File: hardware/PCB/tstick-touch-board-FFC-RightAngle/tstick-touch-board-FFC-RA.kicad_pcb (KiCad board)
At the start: 2 copper layers, 85.6 x 31.8 mm, 14 parts, among them J1 Conn_01x32

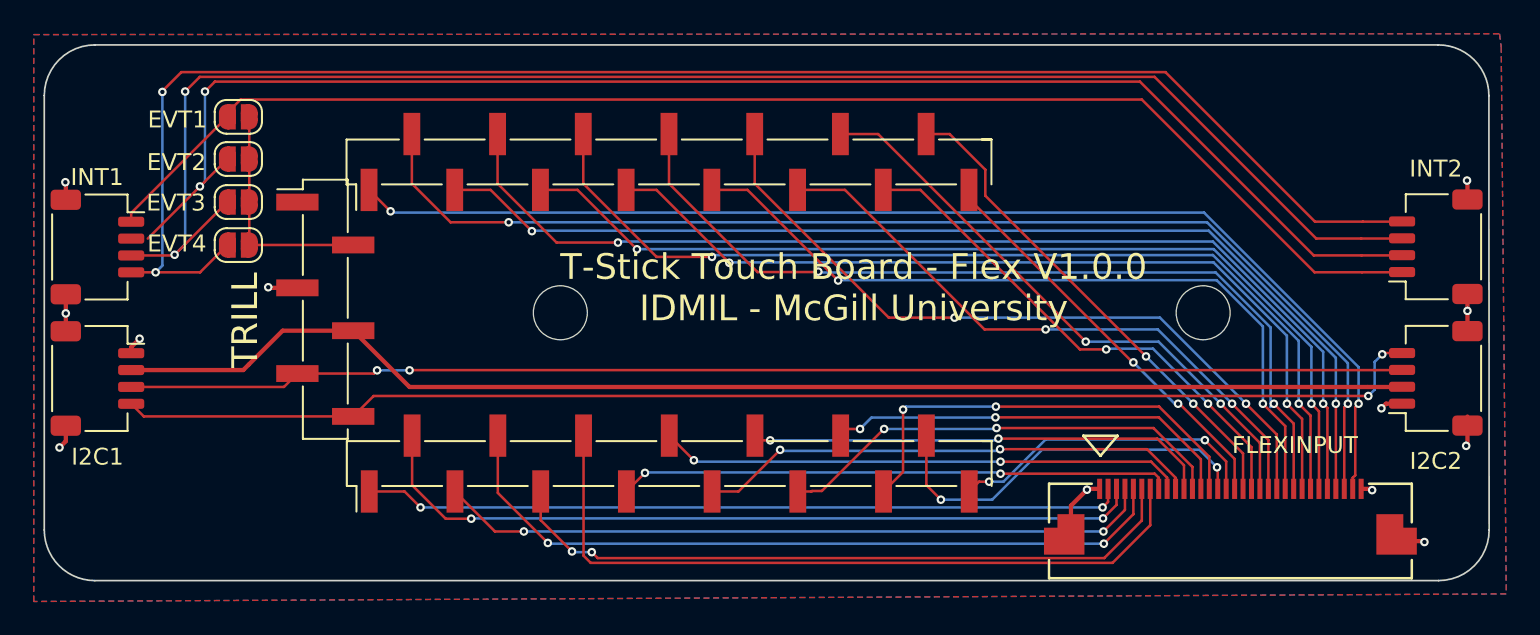
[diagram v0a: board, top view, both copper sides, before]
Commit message: cleaned up v1 of the boards, fixed issue with evt2 trace not being connected in touch board
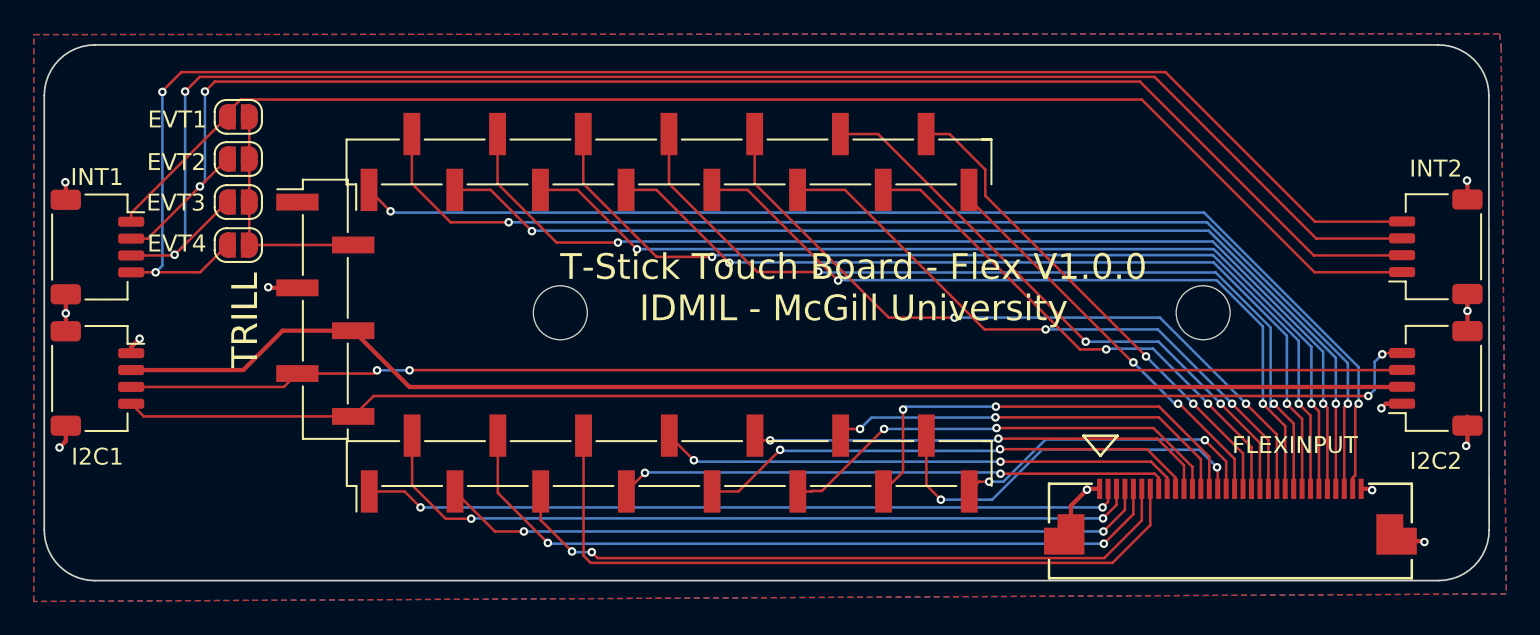
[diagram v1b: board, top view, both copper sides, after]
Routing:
- net /EVT2: track 87.9 -> 88.9 mm
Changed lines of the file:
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@@
     (descr "JST SH series connector, SM04B-SRSS-TB (http://www.jst-mfg.com/product/pdf/eng/eSH.pdf), generated with kicad-footprint-generator")
     (tags "connector JST SH top entry")
+    (property "Alternate Part #" "")
+    (property "Description Value Pkg" "Connector Header Surface Mount, Right Angle 4 position 0.039\" (1.00mm)")
+    (property "Digikey Part #" "455-SM04B-SRSS-TBCT-ND")
+    (property "Mfg Part #" "SM04B-SRSS-TB")
     (property "Sheetfile" "tstick-touch-board-FFC-RA.kicad_sch")
     (property "Sheetname" "")
@@
     (descr "JST SH series connector, SM04B-SRSS-TB (http://www.jst-mfg.com/product/pdf/eng/eSH.pdf), generated with kicad-footprint-generator")
     (tags "connector JST SH top entry")
+    (property "Alternate Part #" "")
+    (property "Description Value Pkg" "Connector Header Surface Mount, Right Angle 4 position 0.039\" (1.00mm)")
+    (property "Digikey Part #" "455-SM04B-SRSS-TBCT-ND")
+    (property "Mfg Part #" "SM04B-SRSS-TB")
     (property "Sheetfile" "tstick-touch-board-FFC-RA.kicad_sch")
     (property "Sheetname" "")
@@
     (descr "JST SH series connector, SM04B-SRSS-TB (http://www.jst-mfg.com/product/pdf/eng/eSH.pdf), generated with kicad-footprint-generator")
     (tags "connector JST SH top entry")
+    (property "Alternate Part #" "")
+    (property "Description Value Pkg" "Connector Header Surface Mount, Right Angle 4 position 0.039\" (1.00mm)")
+    (property "Digikey Part #" "455-SM04B-SRSS-TBCT-ND")
+    (property "Mfg Part #" "SM04B-SRSS-TB")
     (property "Sheetfile" "tstick-touch-board-FFC-RA.kicad_sch")
     (property "Sheetname" "")
@@
     (descr "JST SH series connector, SM04B-SRSS-TB (http://www.jst-mfg.com/product/pdf/eng/eSH.pdf), generated with kicad-footprint-generator")
     (tags "connector JST SH top entry")
+    (property "Alternate Part #" "")
+    (property "Description Value Pkg" "Connector Header Surface Mount, Right Angle 4 position 0.039\" (1.00mm)")
+    (property "Digikey Part #" "455-SM04B-SRSS-TBCT-ND")
+    (property "Mfg Part #" "SM04B-SRSS-TB")
     (property "Sheetfile" "tstick-touch-board-FFC-RA.kicad_sch")
     (property "Sheetname" "")
@@
   (segment (start 144.7697 90.1075) (end 144.7642 90.113) (width 0.1524) (layer "F.Cu") (net 32))
   (segment (start 137.7642 88.213) (end 137.7642 88.729) (width 0.1524) (layer "F.Cu") (net 33))
-  (segment (start 143.3392 82.513) (end 143.4642 82.513) (width 0.1524) (layer "F.Cu") (net 33))
   (segment (start 213.0772 91.725) (end 213.0892 91.713) (width 0.1524) (layer "F.Cu") (net 33))
   (segment (start 144.249002 81.488) (end 143.4642 82.272802) (width 0.1524) (layer "F.Cu") (net 33))
@@
   (segment (start 143.4642 82.513) (end 137.7642 88.213) (width 0.1524) (layer "F.Cu") (net 33))
   (segment (start 197.6642 81.488) (end 144.249002 81.488) (width 0.1524) (layer "F.Cu") (net 33))
-  (segment (start 210.7142 91.725) (end 213.0772 91.725) (width 0.1524) (layer "F.Cu") (net 33))
-  (segment (start 210.7142 91.725) (end 207.9012 91.725) (width 0.1524) (layer "F.Cu") (net 33))
+  (segment (start 207.9012 91.725) (end 213.0772 91.725) (width 0.1524) (layer "F.Cu") (net 33))
   (segment (start 143.4642 82.272802) (end 143.4642 82.513) (width 0.1524) (layer "F.Cu") (net 33))
   (segment (start 142.7264 80.4258) (end 197.552 80.4258) (width 0.1524) (layer "F.Cu") (net 34))
+  (segment (start 138.7482 89.729) (end 137.7642 89.729) (width 0.1524) (layer "F.Cu") (net 34))
   (segment (start 142.1392 81.013) (end 142.7264 80.4258) (width 0.1524) (layer "F.Cu") (net 34))
   (segment (start 141.8392 86.638) (end 138.7482 89.729) (width 0.1524) (layer "F.Cu") (net 34))
   (segment (start 197.552 80.4258) (end 207.8512 90.725) (width 0.1524) (layer "F.Cu") (net 34))
-  (segment (start 210.6892 90.725) (end 213.0772 90.725) (width 0.1524) (layer "F.Cu") (net 34))
-  (segment (start 207.8512 90.725) (end 210.6892 90.725) (width 0.1524) (layer "F.Cu") (net 34))
+  (segment (start 207.8512 90.725) (end 213.0772 90.725) (width 0.1524) (layer "F.Cu") (net 34))
   (segment (start 213.0772 90.725) (end 213.0892 90.713) (width 0.1524) (layer "F.Cu") (net 34))
   (segment (start 141.8392 86.638) (end 143.4642 85.013) (width 0.1524) (layer "F.Cu") (net 34))
@@
   (segment (start 140.9642 81.013) (end 141.8328 80.1444) (width 0.1524) (layer "F.Cu") (net 35))
   (segment (start 140.3392 90.688) (end 143.4642 87.563) (width 0.1524) (layer "F.Cu") (net 35))
-  (segment (start 208.0012 89.725) (end 210.6642 89.725) (width 0.1524) (layer "F.Cu") (net 35))
+  (segment (start 208.0012 89.725) (end 213.0772 89.725) (width 0.1524) (layer "F.Cu") (net 35))
   (segment (start 141.8328 80.1444) (end 198.4206 80.1444) (width 0.1524) (layer "F.Cu") (net 35))
   (segment (start 140.2982 90.729) (end 140.3392 90.688) (width 0.1524) (layer "F.Cu") (net 35))
-  (segment (start 210.6642 89.725) (end 213.0772 89.725) (width 0.1524) (layer "F.Cu") (net 35))
   (segment (start 198.4206 80.1444) (end 208.0012 89.725) (width 0.1524) (layer "F.Cu") (net 35))
   (via (at 140.9642 81.013) (size 0.508) (drill 0.254) (layers "F.Cu" "B.Cu") (net 35))
@@
   (segment (start 140.9642 81.013) (end 140.9642 90.063) (width 0.1524) (layer "B.Cu") (net 35))
   (segment (start 140.9642 90.063) (end 140.3392 90.688) (width 0.1524) (layer "B.Cu") (net 35))
-  (segment (start 210.7642 88.725) (end 213.0772 88.725) (width 0.1524) (layer "F.Cu") (net 36))
+  (segment (start 207.9262 88.725) (end 213.0772 88.725) (width 0.1524) (layer "F.Cu") (net 36))
   (segment (start 141.8482 91.729) (end 143.4642 90.113) (width 0.1524) (layer "F.Cu") (net 36))
   (segment (start 199.0642 79.863) (end 207.9262 88.725) (width 0.1524) (layer "F.Cu") (net 36))
-  (segment (start 207.9262 88.725) (end 210.7642 88.725) (width 0.1524) (layer "F.Cu") (net 36))
   (segment (start 139.6142 81.038) (end 139.6142 80.988) (width 0.1524) (layer "F.Cu") (net 36))
   (segment (start 213.0772 88.725) (end 213.0892 88.713) (width 0.1524) (layer "F.Cu") (net 36))
@@
   (segment (start 139.6142 91.329) (end 139.6142 81.038) (width 0.1524) (layer "B.Cu") (net 36))
   (segment (start 139.2142 91.729) (end 139.6142 91.329) (width 0.1524) (layer "B.Cu") (net 36))
-  (segment (start 144.7392 97.188) (end 146.7397 95.1875) (width 0.254) (layer "F.Cu") (net 37))
+  (segment (start 144.4062 97.521) (end 146.7397 95.1875) (width 0.254) (layer "F.Cu") (net 37))
   (segment (start 146.7397 95.1875) (end 150.925 95.1875) (width 0.254) (layer "F.Cu") (net 37))
-  (segment (start 144.7392 97.188) (end 144.4062 97.521) (width 0.254) (layer "F.Cu") (net 37))
-  (segment (start 154.2625 98.525) (end 211.0642 98.525) (width 0.254) (layer "F.Cu") (net 37))
-  (segment (start 211.0642 98.525) (end 213.0772 98.525) (width 0.254) (layer "F.Cu") (net 37))
+  (segment (start 154.2625 98.525) (end 213.0772 98.525) (width 0.254) (layer "F.Cu") (net 37))
   (segment (start 213.0772 98.525) (end 213.0892 98.513) (width 0.254) (layer "F.Cu") (net 37))
   (segment (start 144.4062 97.521) (end 137.7642 97.521) (width 0.254) (layer "F.Cu") (net 37))
   (segment (start 150.925 95.1875) (end 154.2625 98.525) (width 0.254) (layer "F.Cu") (net 37))
   (segment (start 152.3392 97.538) (end 152.1497 97.7275) (width 0.1524) (layer "F.Cu") (net 38))
-  (segment (start 211.5142 97.525) (end 154.2772 97.525) (width 0.1524) (layer "F.Cu") (net 38))
+  (segment (start 154.2772 97.525) (end 213.0772 97.525) (width 0.1524) (layer "F.Cu") (net 38))
   (segment (start 213.0772 97.525) (end 213.0892 97.513) (width 0.1524) (layer "F.Cu") (net 38))
   (segment (start 146.8215 98.521) (end 147.615 97.7275) (width 0.1524) (layer "F.Cu") (net 38))
-  (segment (start 211.5142 97.525) (end 213.0772 97.525) (width 0.1524) (layer "F.Cu") (net 38))
   (segment (start 152.1497 97.7275) (end 147.615 97.7275) (width 0.1524) (layer "F.Cu") (net 38))
   (segment (start 154.2772 97.525) (end 154.2642 97.538) (width 0.1524) (layer "F.Cu") (net 38))
